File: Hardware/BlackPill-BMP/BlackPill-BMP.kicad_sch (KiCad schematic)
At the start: 39 parts, among them J1 JTAG, J2 VCC, J3 GND, J4 SWO, J5 GDB_COMM, J6 TVCC, J7 LogicAna, J8 Conn_01x10, J9 Conn_01x11, U1 BlueAndBlackPill, U2 AD8531ARTZ, U3 SRV05-4, U4 TXS0108EPW, U5 SRV05-4

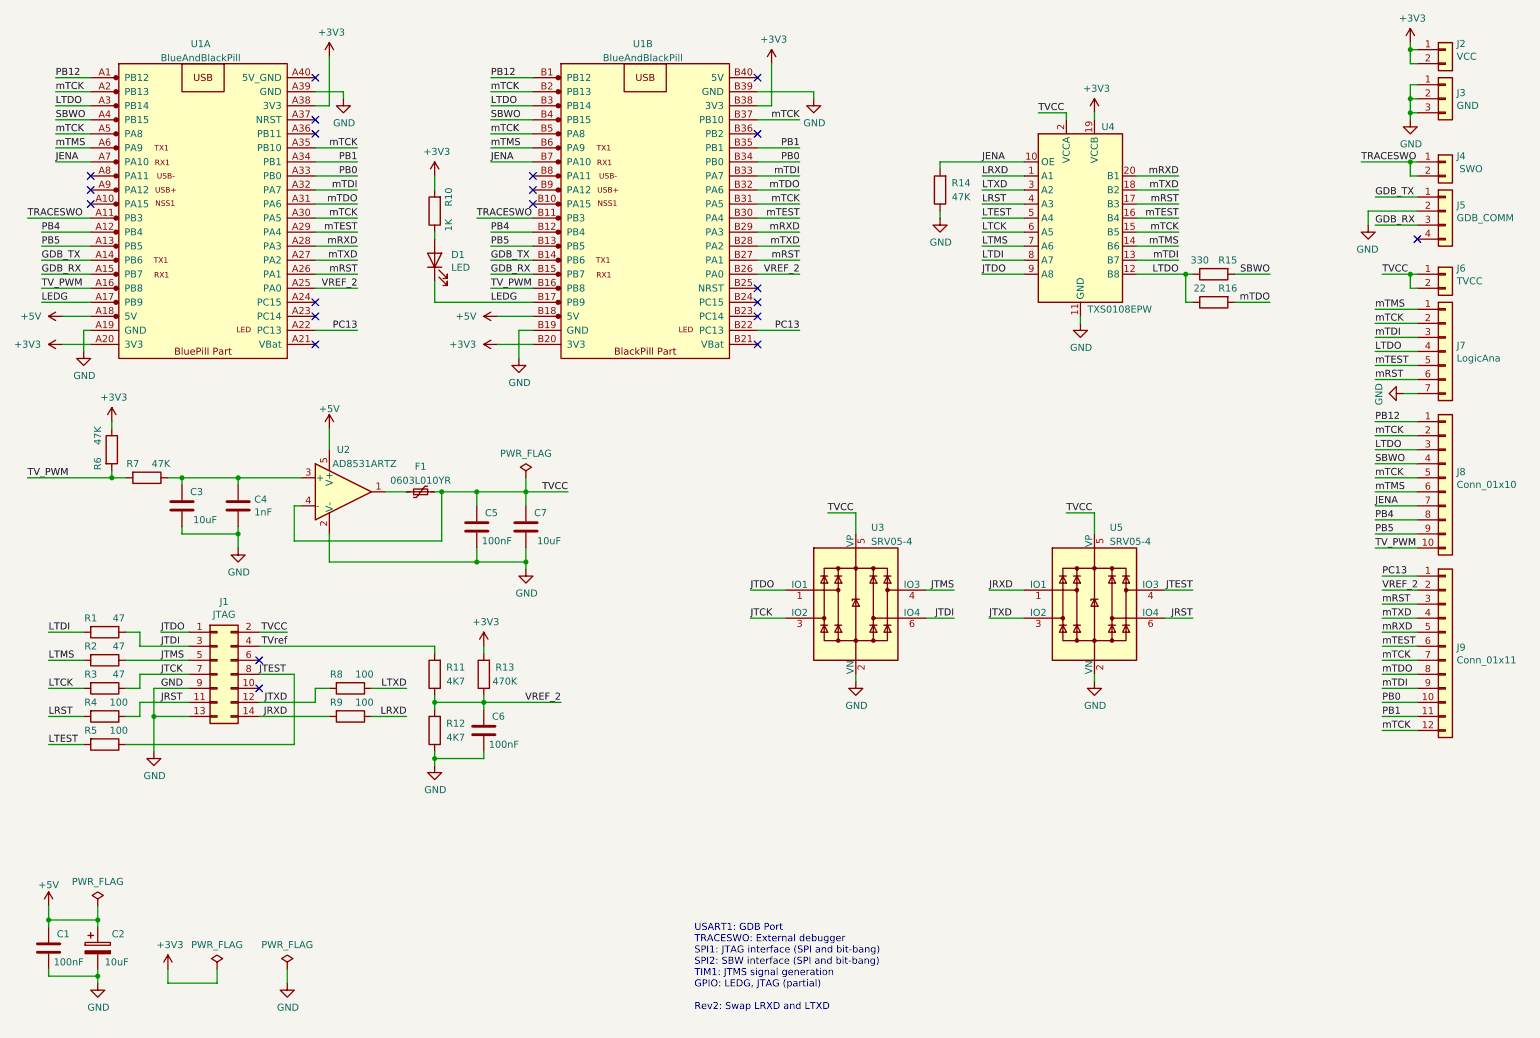
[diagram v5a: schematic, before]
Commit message: Review of ESD protection for Development boards.
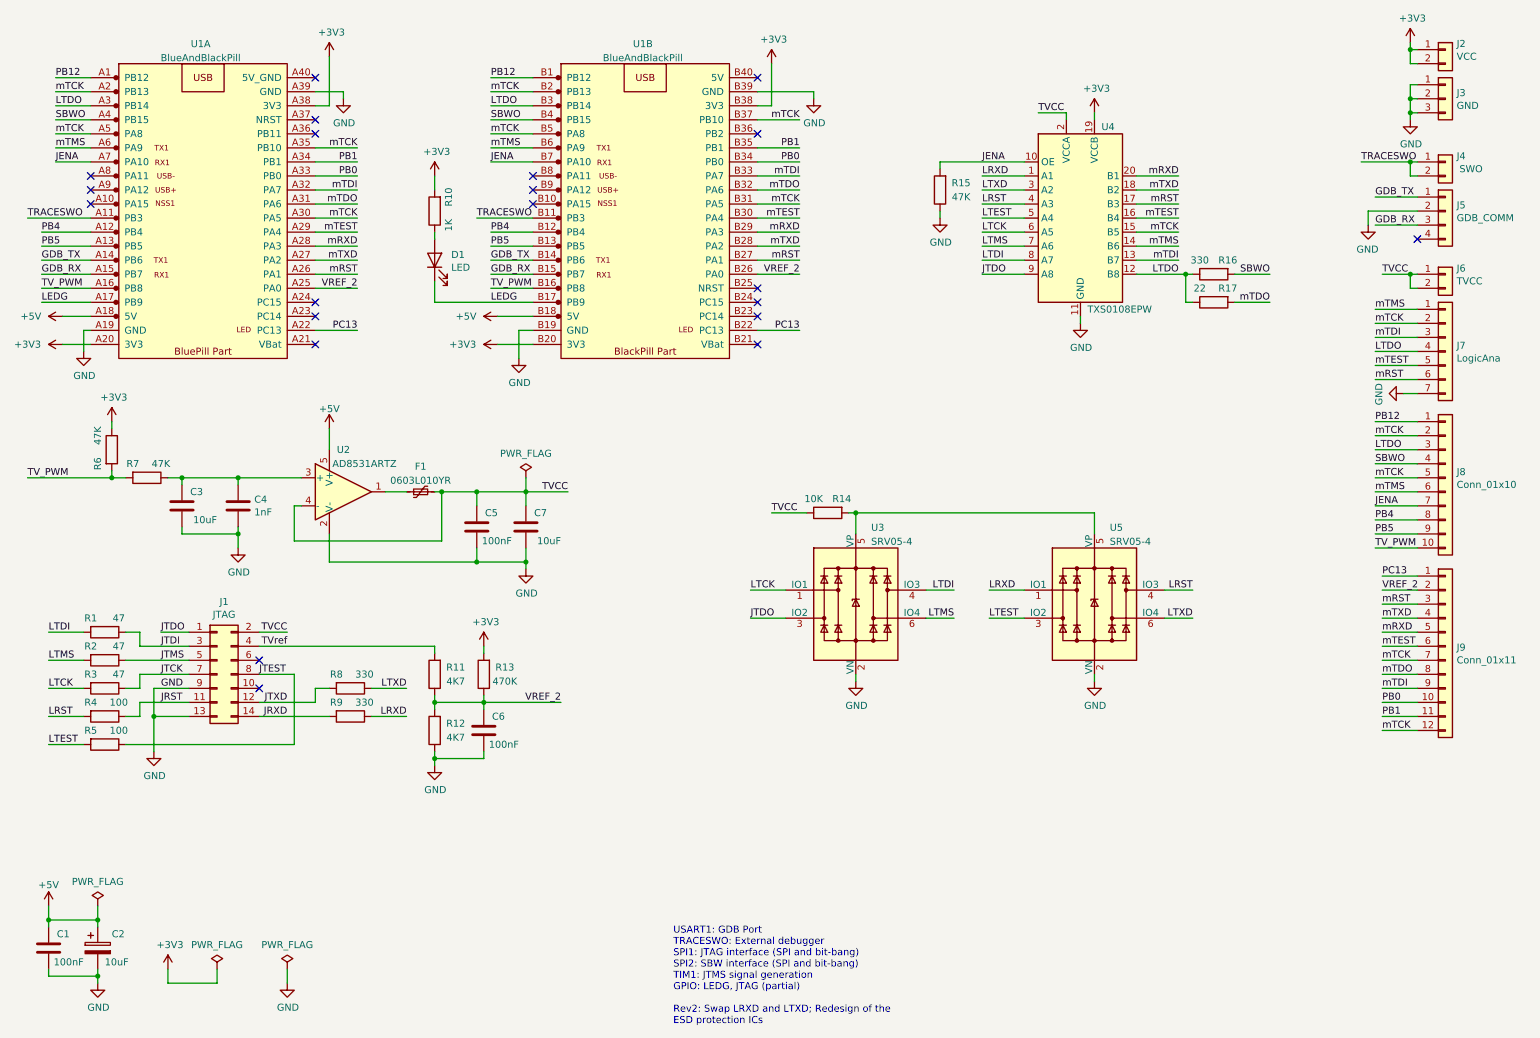
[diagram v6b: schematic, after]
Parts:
- added R14: 10K, Resistor_SMD:R_0603_1608Metric_Pad0.98x0.95mm_HandSolder, symbol Device:R
- R8, R9: value 100 -> 330
- renumbered R14 to R15, R15 to R16, R16 to R17
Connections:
- net JRST: no longer U5.6 (IO4)
- net JRXD: no longer U5.1 (IO1)
- net JTCK: no longer U3.3 (IO2)
- net JTDI: no longer U3.6 (IO4)
- net JTDO: now also U3.3 (IO2); no longer U3.1 (IO1)
- net JTEST: no longer U5.4 (IO3)
- net JTMS: no longer U3.4 (IO3)
- net JTXD: no longer U5.3 (IO2)
- net LRST: now also U5.4 (IO3)
- net LRXD: now also U5.1 (IO1)
- net LTCK: now also U3.1 (IO1)
- net LTDI: now also U3.4 (IO3)
- net LTEST: now also U5.3 (IO2)
- net LTMS: now also U3.6 (IO4)
- net LTXD: now also U5.6 (IO4)
- net TVCC: now also R14.1; no longer U3.5 (VP), U5.5 (VP)
- new net: R14.2, U3.5 (VP), U5.5 (VP)
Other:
- note added: "USART1: GDB Port TRACESWO: External debugger SPI1: JTAG interface (SPI and bit-bang) SPI2: SBW interface (SPI and bit-bang) TIM1: JTMS signal generation GPIO: LEDG, JTAG (partial) Rev2: Swap LRXD and LTXD; Redesign of the ESD protection ICs"
- note removed: "USART1: GDB Port TRACESWO: External debugger SPI1: JTAG interface (SPI and bit-bang) SPI2: SBW interface (SPI and bit-bang) TIM1: JTMS signal generation GPIO: LEDG, JTAG (partial) Rev2: Swap LRXD and LTXD"
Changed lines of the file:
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@@
   (title_block
     (title "MSPBMP Development Protoboard")
-    (date "2022-08-18")
+    (date "2022-08-21")
     (rev "2")
     (company "Mathias Gruber")
@@
   )
   (junction (at 265.43 29.21) (diameter 0) (color 0 0 0 0)
+  )
+  (junction (at 165.1 104.14) (diameter 0) (color 0 0 0 0)
   )
   (junction (at 105.41 113.03) (diameter 0) (color 0 0 0 0)
@@
     (stroke (width 0) (type default) (color 0 0 0 0))
   )
-  (wire (pts (xy 160.02 104.14) (xy 165.1 104.14))
-    (stroke (width 0) (type default) (color 0 0 0 0))
-  )
   (wire (pts (xy 19.05 175.26) (xy 19.05 177.8))
     (stroke (width 0) (type default) (color 0 0 0 0))
@@
     (stroke (width 0) (type default) (color 0 0 0 0))
   )
+  (wire (pts (xy 149.86 104.14) (xy 156.21 104.14))
+    (stroke (width 0) (type default) (color 0 0 0 0))
+  )
   (wire (pts (xy 105.41 113.03) (xy 105.41 114.3))
     (stroke (width 0) (type default) (color 0 0 0 0))
@@
     (stroke (width 0) (type default) (color 0 0 0 0))
   )
+  (wire (pts (xy 163.83 104.14) (xy 165.1 104.14))
+    (stroke (width 0) (type default) (color 0 0 0 0))
+  )
   (wire (pts (xy 147.32 40.64) (xy 154.94 40.64))
     (stroke (width 0) (type default) (color 0 0 0 0))
   )
-  (wire (pts (xy 208.28 104.14) (xy 203.2 104.14))
-    (stroke (width 0) (type default) (color 0 0 0 0))
-  )
   (wire (pts (xy 20.32 35.56) (xy 26.67 35.56))
     (stroke (width 0) (type default) (color 0 0 0 0))
@@
     (stroke (width 0) (type default) (color 0 0 0 0))
   )
+  (wire (pts (xy 165.1 104.14) (xy 208.28 104.14))
+    (stroke (width 0) (type default) (color 0 0 0 0))
+  )
   (wire (pts (xy 88.9 138.43) (xy 97.79 138.43))
     (stroke (width 0) (type default) (color 0 0 0 0))
@@
     (stroke (width 0) (type default) (color 0 0 0 0))
   )
-  (text "USART1: GDB Port\nTRACESWO: External debugger\nSPI1: JTAG interface (SPI and bit-bang)\nSPI2: SBW interface (SPI and bit-bang)\nTIM1: JTMS signal generation\nGPIO: LEDG, JTAG (partial)\n\nRev2: Swap LRXD and LTXD"
-    (at 135.89 194.31 0)
+  (text "USART1: GDB Port\nTRACESWO: External debugger\nSPI1: JTAG interface (SPI and bit-bang)\nSPI2: SBW interface (SPI and bit-bang)\nTIM1: JTMS signal generation\nGPIO: LEDG, JTAG (partial)\n\nRev2: Swap LRXD and LTXD; Redesign of the \nESD protection ICs"
+    (at 132.08 196.85 0)
     (effects (font (size 1.27 1.27)) (justify left bottom))
   )
@@
     (effects (font (size 1.27 1.27)) (justify right bottom))
   )
-  (label "JRST" (at 226.06 123.19 180)
+  (label "LRST" (at 226.06 118.11 180)
     (effects (font (size 1.27 1.27)) (justify right bottom))
   )
@@
     (effects (font (size 1.27 1.27)) (justify right bottom))
   )
-  (label "JRXD" (at 189.23 118.11 0)
+  (label "LRXD" (at 189.23 118.11 0)
     (effects (font (size 1.27 1.27)) (justify left bottom))
   )
@@
     (effects (font (size 1.27 1.27)) (justify left bottom))
   )
-  (label "JTEST" (at 226.06 118.11 180)
-    (effects (font (size 1.27 1.27)) (justify right bottom))
+  (label "LTEST" (at 189.23 123.19 0)
+    (effects (font (size 1.27 1.27)) (justify left bottom))
   )
   (label "mTEST" (at 223.52 50.8 180)
@@
     (effects (font (size 1.27 1.27)) (justify left bottom))
   )
-  (label "JTDI" (at 182.88 123.19 180)
+  (label "LTDI" (at 182.88 118.11 180)
     (effects (font (size 1.27 1.27)) (justify right bottom))
   )
@@
     (effects (font (size 1.27 1.27)) (justify right bottom))
   )
-  (label "JTDO" (at 146.05 118.11 0)
+  (label "JTDO" (at 146.05 123.19 0)
     (effects (font (size 1.27 1.27)) (justify left bottom))
   )
@@
     (effects (font (size 1.27 1.27)) (justify left bottom))
   )
-  (label "JTXD" (at 189.23 123.19 0)
-    (effects (font (size 1.27 1.27)) (justify left bottom))
+  (label "LTXD" (at 226.06 123.19 180)
+    (effects (font (size 1.27 1.27)) (justify right bottom))
   )
   (label "LRST" (at 187.96 48.26 0)
     (effects (font (size 1.27 1.27)) (justify left bottom))
   )
-  (label "JTMS" (at 182.88 118.11 180)
+  (label "LTMS" (at 182.88 123.19 180)
     (effects (font (size 1.27 1.27)) (justify right bottom))
   )
@@
     (effects (font (size 1.27 1.27)) (justify left bottom))
   )
-  (label "TVCC" (at 160.02 104.14 0)
+  (label "TVCC" (at 149.86 104.14 0)
     (effects (font (size 1.27 1.27)) (justify left bottom))
   )
@@
     (effects (font (size 1.27 1.27)) (justify left bottom))
   )
-  (label "TVCC" (at 203.2 104.14 0)
-    (effects (font (size 1.27 1.27)) (justify left bottom))
-  )
   (label "SBWO" (at 240.03 60.96 180)
     (effects (font (size 1.27 1.27)) (justify right bottom))
@@
     (effects (font (size 1.27 1.27)) (justify right bottom))
   )
-  (label "JTCK" (at 146.05 123.19 0)
+  (label "LTCK" (at 146.05 118.11 0)
     (effects (font (size 1.27 1.27)) (justify left bottom))
   )
@@
   (symbol (lib_id "Device:R") (at 229.87 66.04 90) (mirror x) (unit 1)
     (in_bom yes) (on_board yes)
-    (property "Reference" "R16" (id 0) (at 232.41 63.5 90))
+    (property "Reference" "R17" (id 0) (at 232.41 63.5 90))
     (property "Value" "22" (id 1) (at 227.33 63.5 90))
     (property "Footprint" "Resistor_SMD:R_0603_1608Metric_Pad0.98x0.95mm_HandSolder" (id 2) (at 229.87 64.262 90)
@@
     (in_bom yes) (on_board yes)
     (property "Reference" "R8" (id 0) (at 71.12 133.35 90))
-    (property "Value" "100" (id 1) (at 76.2 133.35 90))
+    (property "Value" "330" (id 1) (at 76.2 133.35 90))
     (property "Footprint" "Resistor_SMD:R_0603_1608Metric_Pad0.98x0.95mm_HandSolder" (id 2) (at 73.66 134.112 90)
       (effects (font (size 1.27 1.27)) hide)
@@
     (in_bom yes) (on_board yes)
     (property "Reference" "R9" (id 0) (at 71.12 138.43 90))
-    (property "Value" "100" (id 1) (at 76.2 138.43 90))
+    (property "Value" "330" (id 1) (at 76.2 138.43 90))
     (property "Footprint" "Resistor_SMD:R_0603_1608Metric_Pad0.98x0.95mm_HandSolder" (id 2) (at 73.66 139.192 90)
       (effects (font (size 1.27 1.27)) hide)
@@
   (symbol (lib_id "Device:R") (at 229.87 60.96 90) (mirror x) (unit 1)
     (in_bom yes) (on_board yes)
-    (property "Reference" "R15" (id 0) (at 232.41 58.42 90))
+    (property "Reference" "R16" (id 0) (at 232.41 58.42 90))
     (property "Value" "330" (id 1) (at 227.33 58.42 90))
     (property "Footprint" "Resistor_SMD:R_0603_1608Metric_Pad0.98x0.95mm_HandSolder" (id 2) (at 229.87 59.182 90)
@@
     )
     (pin "1")
+  )
+  (symbol (lib_id "Device:R") (at 160.02 104.14 90) (mirror x) (unit 1)
+    (in_bom yes) (on_board yes)
+    (property "Reference" "R14" (id 0) (at 162.56 101.6 90))
+    (property "Value" "10K" (id 1) (at 157.48 101.6 90))
+    (property "Footprint" "Resistor_SMD:R_0603_1608Metric_Pad0.98x0.95mm_HandSolder" (id 2) (at 160.02 102.362 90)
+      (effects (font (size 1.27 1.27)) hide)
+    )
+    (property "Datasheet" "~" (id 3) (at 160.02 104.14 0)
+      (effects (font (size 1.27 1.27)) hide)
+    )
+    (pin "1")
+    (pin "2")
   )
   (symbol (lib_id "Device:Polyfuse_Small") (at 86.36 100.33 90) (unit 1)
@@
   (symbol (lib_id "Device:R") (at 180.34 45.72 180) (unit 1)
     (in_bom yes) (on_board yes)
-    (property "Reference" "R14" (id 0) (at 184.15 44.45 0))
+    (property "Reference" "R15" (id 0) (at 184.15 44.45 0))
     (property "Value" "47K" (id 1) (at 184.15 46.99 0))
     (property "Footprint" "Resistor_SMD:R_0603_1608Metric_Pad0.98x0.95mm_HandSolder" (id 2) (at 182.118 45.72 90)
@@
     )
     (path "/00000000-0000-0000-0000-000061b80bd6"
-      (reference "R8") (unit 1) (value "100") (footprint "Resistor_SMD:R_0603_1608Metric_Pad0.98x0.95mm_HandSolder")
+      (reference "R8") (unit 1) (value "330") (footprint "Resistor_SMD:R_0603_1608Metric_Pad0.98x0.95mm_HandSolder")
     )
     (path "/00000000-0000-0000-0000-000061b88e56"
-      (reference "R9") (unit 1) (value "100") (footprint "Resistor_SMD:R_0603_1608Metric_Pad0.98x0.95mm_HandSolder")
+      (reference "R9") (unit 1) (value "330") (footprint "Resistor_SMD:R_0603_1608Metric_Pad0.98x0.95mm_HandSolder")
     )
     (path "/00000000-0000-0000-0000-00006186facf"
@@
       (reference "R13") (unit 1) (value "470K") (footprint "Resistor_SMD:R_0603_1608Metric_Pad0.98x0.95mm_HandSolder")
     )
+    (path "/37e00f67-31ad-4159-be93-826c8f0048f5"
+      (reference "R14") (unit 1) (value "10K") (footprint "Resistor_SMD:R_0603_1608Metric_Pad0.98x0.95mm_HandSolder")
+    )
     (path "/f130f0f6-9f20-4a51-b79e-b456b8b84272"
-      (reference "R14") (unit 1) (value "47K") (footprint "Resistor_SMD:R_0603_1608Metric_Pad0.98x0.95mm_HandSolder")
+      (reference "R15") (unit 1) (value "47K") (footprint "Resistor_SMD:R_0603_1608Metric_Pad0.98x0.95mm_HandSolder")
     )
     (path "/20e94b95-8d09-4e42-a292-6210a8afcf50"
-      (reference "R15") (unit 1) (value "330") (footprint "Resistor_SMD:R_0603_1608Metric_Pad0.98x0.95mm_HandSolder")
+      (reference "R16") (unit 1) (value "330") (footprint "Resistor_SMD:R_0603_1608Metric_Pad0.98x0.95mm_HandSolder")
     )
     (path "/00000000-0000-0000-0000-0000619ec4b5"
-      (reference "R16") (unit 1) (value "22") (footprint "Resistor_SMD:R_0603_1608Metric_Pad0.98x0.95mm_HandSolder")
+      (reference "R17") (unit 1) (value "22") (footprint "Resistor_SMD:R_0603_1608Metric_Pad0.98x0.95mm_HandSolder")
     )
     (path "/b141b0b5-1c34-438f-8f5a-a2e1dda2ee83"
